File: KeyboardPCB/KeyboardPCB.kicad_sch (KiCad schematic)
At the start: 2 parts

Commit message: Made progress on keyboard schematic
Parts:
- added C? (x3): C, symbol Device:C
- added R? (x4): R, symbol Device:R
- added SW?: SW_Push, symbol Switch:SW_Push
- added Y?: Crystal_GND24_Small, symbol Device:Crystal_GND24_Small
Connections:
- net GND: now also U?.5 (UGND), C?.2, C?.2, C?.2, R?.1, SW?.1
- net at P?.A4 (VBUS), P?.A9 (VBUS), P?.B4 (VBUS)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: now also U?.2 (UVCC), U?.24 (AVCC), U?.44 (AVCC)
- net at U?.4 (D+): now also R?.1; no longer P?.A6 (D+)
- net at P?.A7 (D-): now also R?.2; no longer U?.3 (D-)
- net COL10: now reaches U?.1 (PE6)
- net COL1: now reaches U?.10 (PB2)
- net COL0: now reaches U?.11 (PB3)
- net ROW0: now reaches U?.12 (PB7)
- net at U?.13 (~{RESET}): now also R?.2
- net at U?.16 (XTAL2): now also C?.1, Y?.1
- net at U?.17 (XTAL1): now also C?.1, Y?.3
- net COL9: now reaches U?.18 (PD0)
- net COL8: now reaches U?.19 (PD1)
- net COL7: now reaches U?.20 (PD2)
- net COL6: now reaches U?.21 (PD3)
- net COL5: now reaches U?.22 (PD5)
- net COL19: now reaches U?.25 (PD4)
- net COL18: now reaches U?.26 (PD6)
- net COL17: now reaches U?.27 (PD7)
- net COL16: now reaches U?.28 (PB4)
- net COL15: now reaches U?.29 (PB5)
- net COL14: now reaches U?.30 (PB6)
- net COL13: now reaches U?.31 (PC6)
- net COL12: now reaches U?.32 (PC7)
- net at U?.33 (~{HWB}/PE2): now also R?.2
- net COL4: now reaches U?.36 (PF7)
- net ROW2: now reaches U?.37 (PF6)
- net ROW3: now reaches U?.38 (PF5)
- net ROW4: now reaches U?.39 (PF4)
- net ROW1: now reaches U?.40 (PF1)
- net COL11: now reaches U?.41 (PF0)
- net at U?.6 (UCAP): now also C?.1
- net COL3: now reaches U?.8 (PB0)
- net COL2: now reaches U?.9 (PB1)
- new net: R?.1, SW?.2
- new net: P?.A6 (D+), R?.2
- new net: R?.1, U?.3 (D-)
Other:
- moved on the sheet: P?, U?

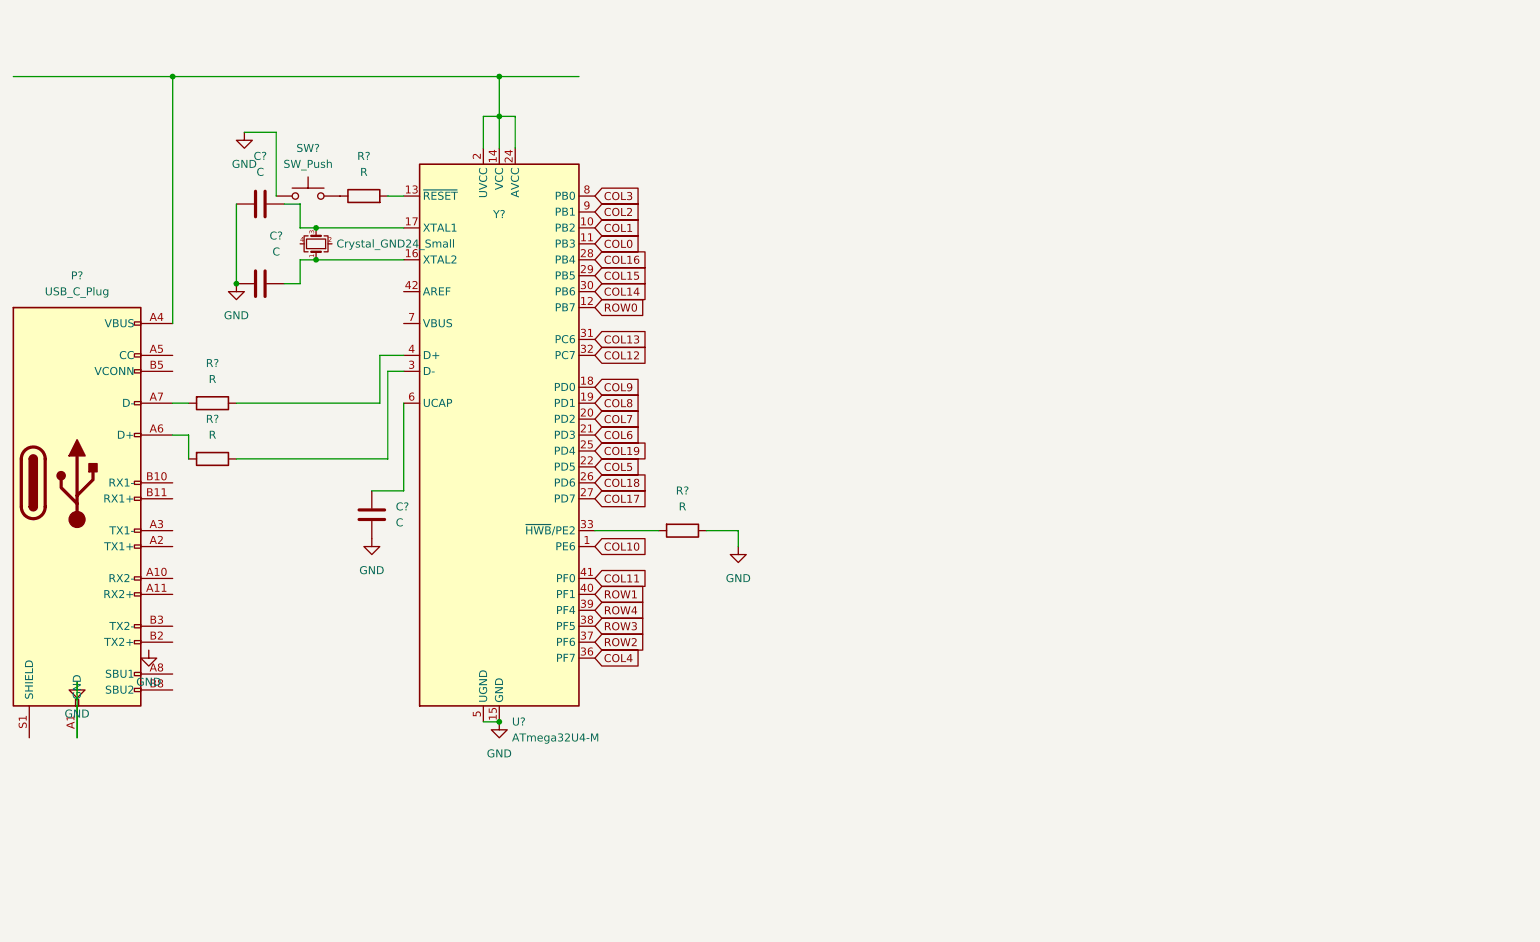
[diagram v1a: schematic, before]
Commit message: Added Sheets for main MCU/battery and key array
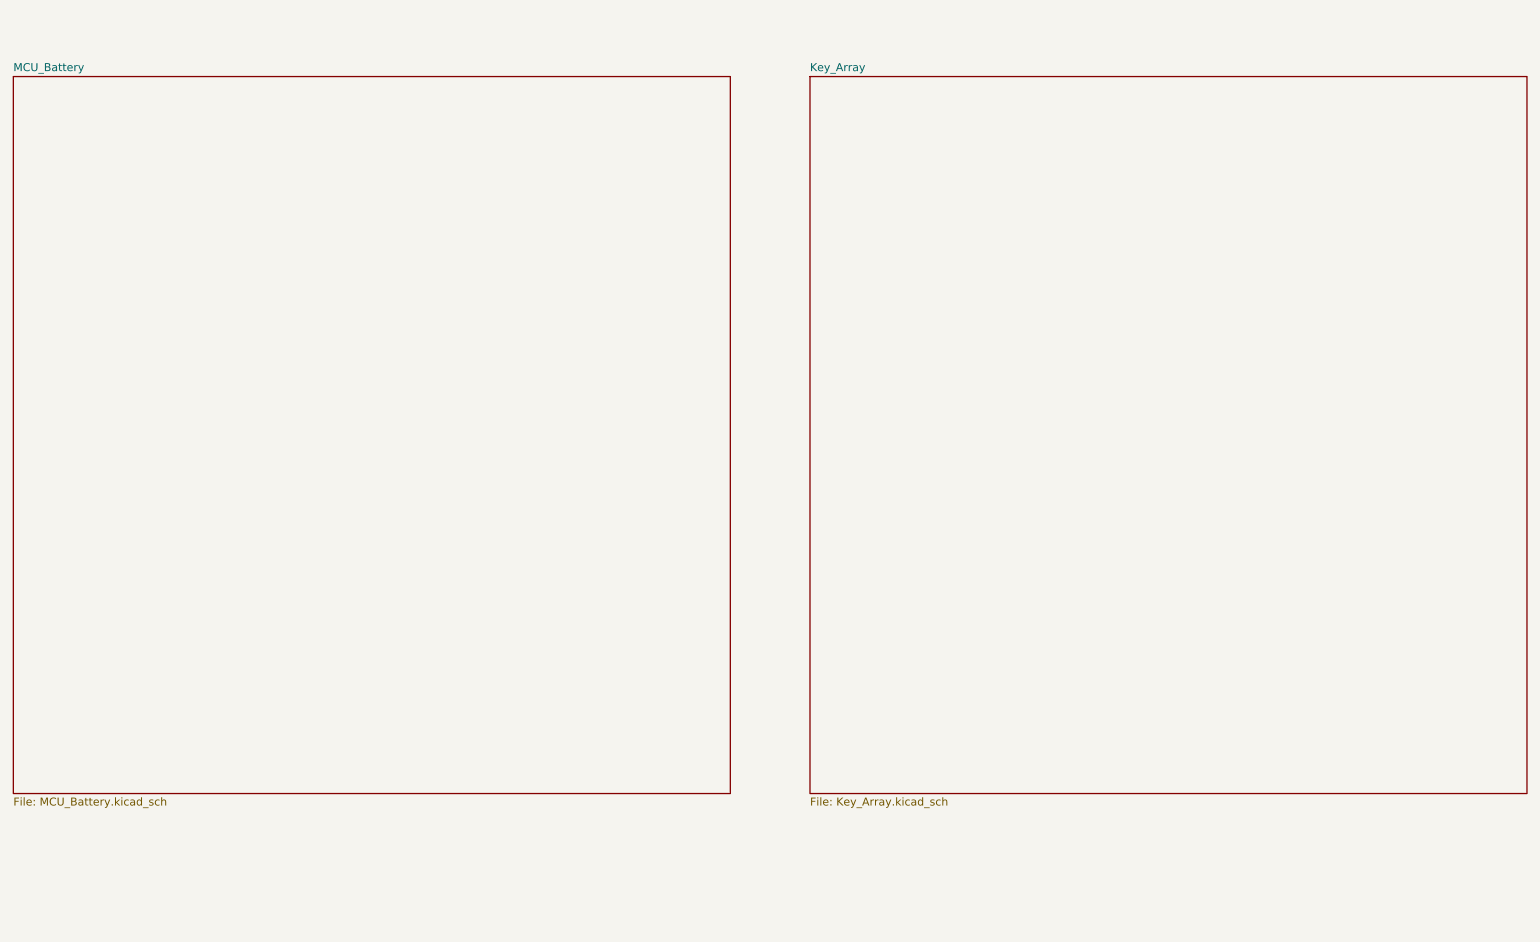
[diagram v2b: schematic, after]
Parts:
- removed C? (x3): C, symbol Device:C
- removed P?: USB_C_Plug, symbol Connector:USB_C_Plug
- removed R? (x4): R, symbol Device:R
- removed SW?: SW_Push, symbol Switch:SW_Push
- removed U?: ATmega32U4-M, Package_DFN_QFN:QFN-44-1EP_7x7mm_P0.5mm_EP5.2x5.2mm, symbol MCU_Microchip_ATmega:ATmega32U4-M
- removed Y?: Crystal_GND24_Small, symbol Device:Crystal_GND24_Small
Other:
- added sheet Key_Array (Key_Array.kicad_sch)
- added sheet MCU_Battery (MCU_Battery.kicad_sch)

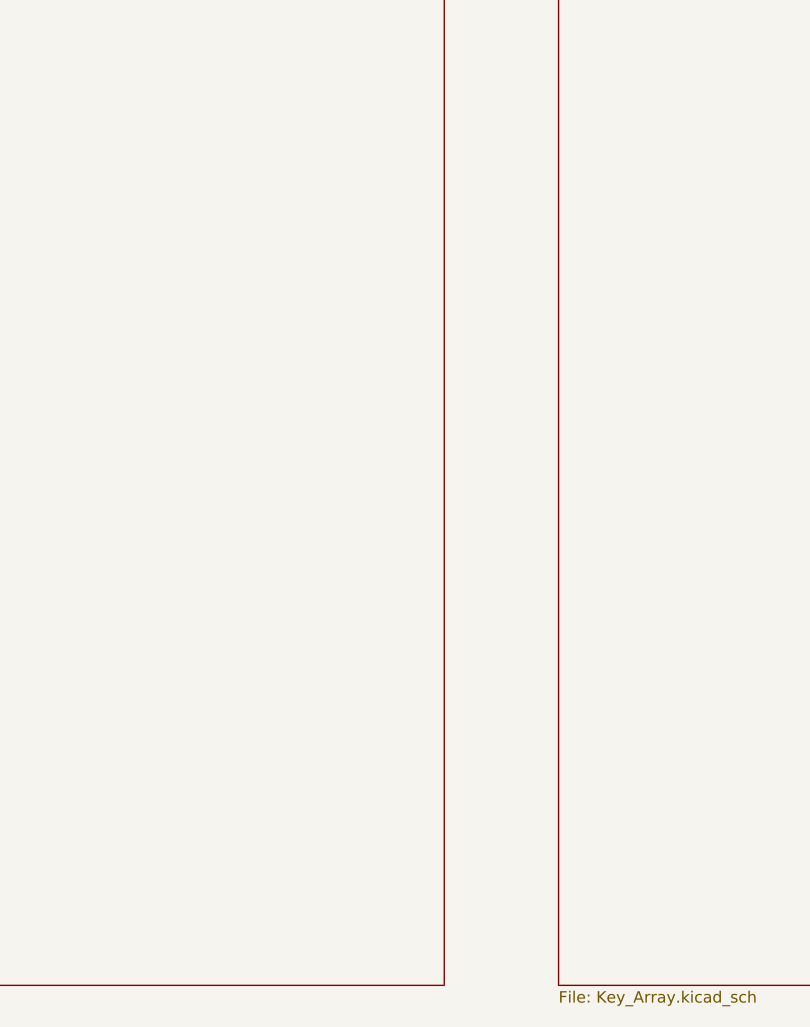
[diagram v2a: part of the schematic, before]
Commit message: set up for key array
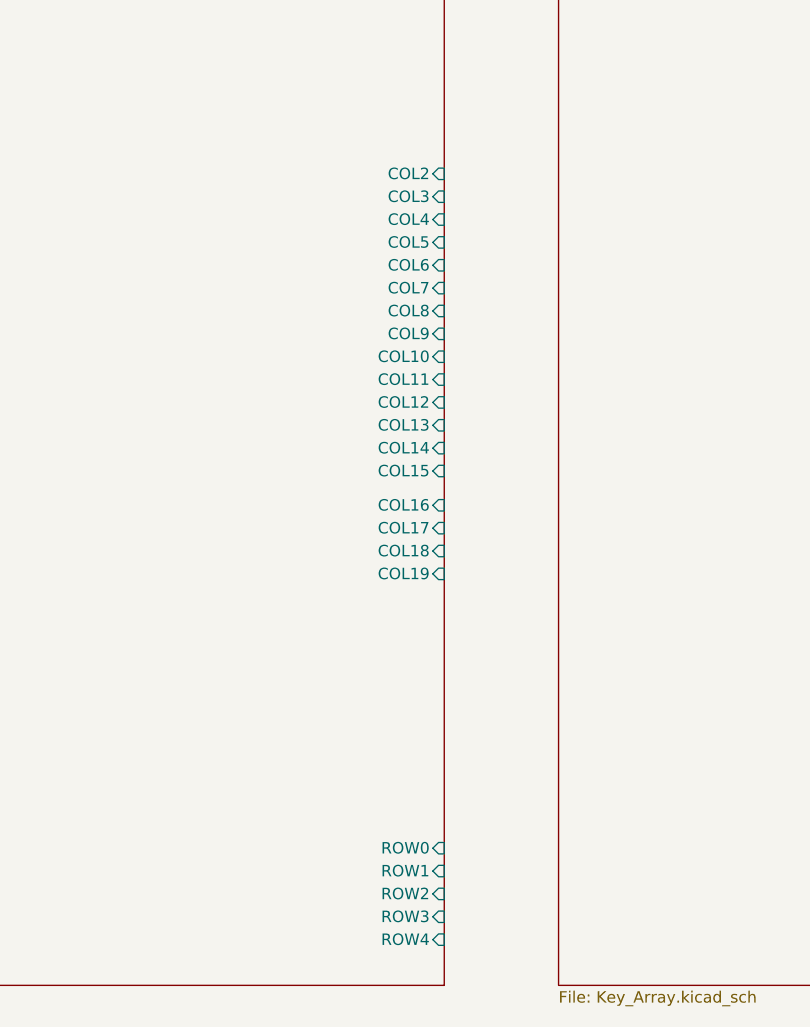
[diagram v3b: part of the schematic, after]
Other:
- sheet MCU_Battery ports: added COL10, COL11, COL12, COL13, COL14, COL15, COL16, COL17, COL18, COL19, COL2, COL3, COL4, COL5, COL6, COL7, COL8, COL9, ROW0, ROW1, ROW2, ROW3, ROW4; removed none
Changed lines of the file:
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@@
       (effects (font (size 1.27 1.27)) (justify left top))
+    )
+    (pin "COL3" input (at 139.7 52.07 0)
+      (effects (font (size 1.27 1.27)) (justify right))
+    )
+    (pin "ROW4" input (at 139.7 134.62 0)
+      (effects (font (size 1.27 1.27)) (justify right))
+    )
+    (pin "ROW1" input (at 139.7 127 0)
+      (effects (font (size 1.27 1.27)) (justify right))
+    )
+    (pin "COL11" input (at 139.7 72.39 0)
+      (effects (font (size 1.27 1.27)) (justify right))
+    )
+    (pin "COL18" input (at 139.7 91.44 0)
+      (effects (font (size 1.27 1.27)) (justify right))
+    )
+    (pin "COL10" input (at 139.7 69.85 0)
+      (effects (font (size 1.27 1.27)) (justify right))
+    )
+    (pin "COL17" input (at 139.7 88.9 0)
+      (effects (font (size 1.27 1.27)) (justify right))
+    )
+    (pin "COL5" input (at 139.7 57.15 0)
+      (effects (font (size 1.27 1.27)) (justify right))
+    )
+    (pin "COL7" input (at 139.7 62.23 0)
+      (effects (font (size 1.27 1.27)) (justify right))
+    )
+    (pin "COL6" input (at 139.7 59.69 0)
+      (effects (font (size 1.27 1.27)) (justify right))
+    )
+    (pin "COL19" input (at 139.7 93.98 0)
+      (effects (font (size 1.27 1.27)) (justify right))
+    )
+    (pin "COL8" input (at 139.7 64.77 0)
+      (effects (font (size 1.27 1.27)) (justify right))
+    )
+    (pin "ROW3" input (at 139.7 132.08 0)
+      (effects (font (size 1.27 1.27)) (justify right))
+    )
+    (pin "COL4" input (at 139.7 54.61 0)
+      (effects (font (size 1.27 1.27)) (justify right))
+    )
+    (pin "ROW2" input (at 139.7 129.54 0)
+      (effects (font (size 1.27 1.27)) (justify right))
+    )
+    (pin "ROW0" input (at 139.7 124.46 0)
+      (effects (font (size 1.27 1.27)) (justify right))
+    )
+    (pin "COL9" input (at 139.7 67.31 0)
+      (effects (font (size 1.27 1.27)) (justify right))
+    )
+    (pin "COL13" input (at 139.7 77.47 0)
+      (effects (font (size 1.27 1.27)) (justify right))
+    )
+    (pin "COL12" input (at 139.7 74.93 0)
+      (effects (font (size 1.27 1.27)) (justify right))
+    )
+    (pin "COL16" input (at 139.7 86.36 0)
+      (effects (font (size 1.27 1.27)) (justify right))
+    )
+    (pin "COL2" input (at 139.7 49.53 0)
+      (effects (font (size 1.27 1.27)) (justify right))
+    )
+    (pin "COL14" input (at 139.7 80.01 0)
+      (effects (font (size 1.27 1.27)) (justify right))
+    )
+    (pin "COL15" input (at 139.7 82.55 0)
+      (effects (font (size 1.27 1.27)) (justify right))
     )
   )
@@
       (reference "#PWR?") (unit 1) (value "GND") (footprint "")
     )
-    (path "/0e04ce72-6533-49cc-b4b5-6fa7ba1a6887/e65c3227-a683-4185-b179-fe03d95c6a0f"
-      (reference "#PWR?") (unit 1) (value "GND") (footprint "")
-    )
     (path "/0e04ce72-6533-49cc-b4b5-6fa7ba1a6887/f025268d-94e6-435c-9e99-144e0a25759e"
       (reference "#PWR?") (unit 1) (value "GND") (footprint "")
     )
+    (path "/0e04ce72-6533-49cc-b4b5-6fa7ba1a6887/f72b91bb-4963-49bc-9a06-44650fc96a66"
+      (reference "#PWR?") (unit 1) (value "GND") (footprint "")
+    )

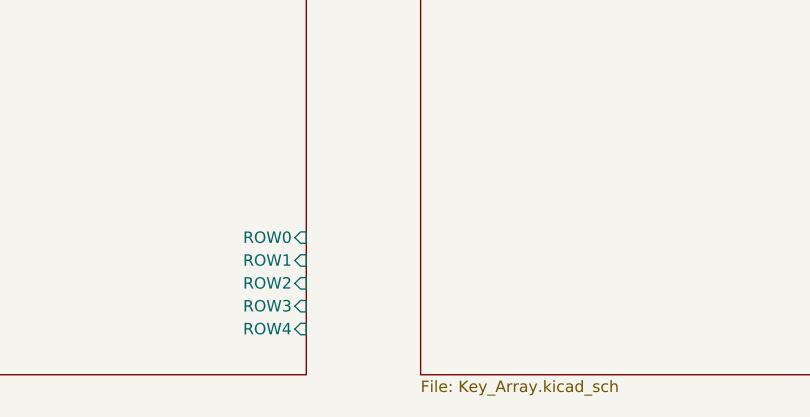
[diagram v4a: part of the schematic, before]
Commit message: keyboard added
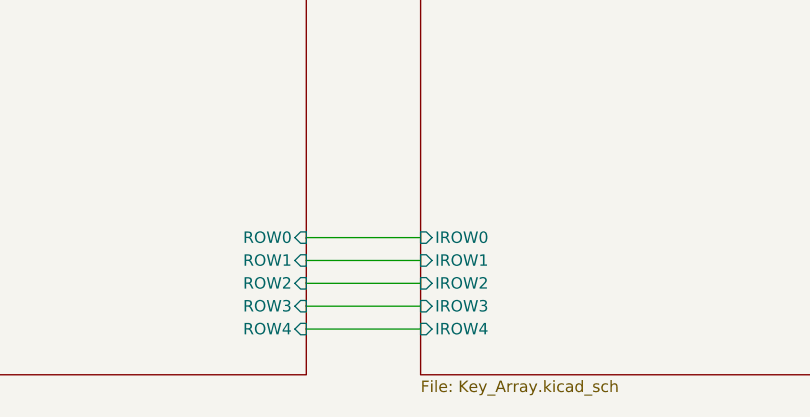
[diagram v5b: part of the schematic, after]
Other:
- sheet Key_Array ports: added IROW0, IROW1, IROW2, IROW3, IROW4; removed none
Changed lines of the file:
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@@
 (kicad_sch (version 20211123) (generator eeschema)
   (paper "A4")
+  (wire (pts (xy 139.7 129.54) (xy 152.4 129.54))
+    (stroke (width 0) (type default) (color 0 0 0 0))
+  )
+  (wire (pts (xy 139.7 127) (xy 152.4 127))
+    (stroke (width 0) (type default) (color 0 0 0 0))
+  )
+  (wire (pts (xy 139.7 134.62) (xy 152.4 134.62))
+    (stroke (width 0) (type default) (color 0 0 0 0))
+  )
+  (wire (pts (xy 139.7 132.08) (xy 152.4 132.08))
+    (stroke (width 0) (type default) (color 0 0 0 0))
+  )
+  (wire (pts (xy 139.7 124.46) (xy 152.4 124.46))
+    (stroke (width 0) (type default) (color 0 0 0 0))
+  )
   (sheet (at 25.4 25.4) (size 114.3 114.3) (fields_autoplaced)
     (stroke (width 0.1524) (type solid) (color 0 0 0 0))
@@
       (effects (font (size 1.27 1.27)) (justify left top))
     )
+    (pin "IROW3" input (at 152.4 132.08 180)
+      (effects (font (size 1.27 1.27)) (justify left))
+    )
+    (pin "IROW0" input (at 152.4 124.46 180)
+      (effects (font (size 1.27 1.27)) (justify left))
+    )
+    (pin "IROW1" input (at 152.4 127 180)
+      (effects (font (size 1.27 1.27)) (justify left))
+    )
+    (pin "IROW2" input (at 152.4 129.54 180)
+      (effects (font (size 1.27 1.27)) (justify left))
+    )
+    (pin "IROW4" input (at 152.4 134.62 180)
+      (effects (font (size 1.27 1.27)) (justify left))
+    )
   )
   (sheet_instances
@@
       (reference "C?") (unit 1) (value "C") (footprint "")
     )
+    (path "/ea7fdac0-4451-48b5-bbfd-e0f47d60ba04/085d0668-2bdd-442e-845c-04885261abc3"
+      (reference "D?") (unit 1) (value "1N4148WT") (footprint "Diode_SMD:D_SOD-523")
+    )
+    (path "/ea7fdac0-4451-48b5-bbfd-e0f47d60ba04/093654b7-9a4e-46ae-aec2-41e4a1ffa408"
+      (reference "D?") (unit 1) (value "1N4148WT") (footprint "Diode_SMD:D_SOD-523")
+    )
+    (path "/ea7fdac0-4451-48b5-bbfd-e0f47d60ba04/0d494db2-e686-41d9-88ce-34916737d604"
+      (reference "D?") (unit 1) (value "1N4148WT") (footprint "Diode_SMD:D_SOD-523")
+    )
+    (path "/ea7fdac0-4451-48b5-bbfd-e0f47d60ba04/16056eea-bff8-43e3-bb4c-e2e99df660e6"
+      (reference "D?") (unit 1) (value "1N4148WT") (footprint "Diode_SMD:D_SOD-523")
+    )
+    (path "/ea7fdac0-4451-48b5-bbfd-e0f47d60ba04/17a0798e-831d-48ea-bd0e-a352003521db"
+      (reference "D?") (unit 1) (value "1N4148WT") (footprint "Diode_SMD:D_SOD-523")
+    )
+    (path "/ea7fdac0-4451-48b5-bbfd-e0f47d60ba04/223d0d00-e7b6-435c-969f-835885c93655"
+      (reference "D?") (unit 1) (value "1N4148WT") (footprint "Diode_SMD:D_SOD-523")
+    )
+    (path "/ea7fdac0-4451-48b5-bbfd-e0f47d60ba04/41cf5a6e-7eaf-4a99-af9a-7c6d950a495f"
+      (reference "D?") (unit 1) (value "1N4148WT") (footprint "Diode_SMD:D_SOD-523")
+    )
+    (path "/ea7fdac0-4451-48b5-bbfd-e0f47d60ba04/431e94e4-692a-49ef-91fa-2f1556593f4e"
+      (reference "D?") (unit 1) (value "1N4148WT") (footprint "Diode_SMD:D_SOD-523")
+    )
+    (path "/ea7fdac0-4451-48b5-bbfd-e0f47d60ba04/501e12a6-9a36-4baf-80f5-810ca392bffd"
+      (reference "D?") (unit 1) (value "1N4148WT") (footprint "Diode_SMD:D_SOD-523")
+    )
+    (path "/ea7fdac0-4451-48b5-bbfd-e0f47d60ba04/5840ce00-bee4-40ba-846f-10ca1bb7d4de"
+      (reference "D?") (unit 1) (value "1N4148WT") (footprint "Diode_SMD:D_SOD-523")
+    )
+    (path "/ea7fdac0-4451-48b5-bbfd-e0f47d60ba04/5fa281b3-e577-4328-8d83-48a007938557"
+      (reference "D?") (unit 1) (value "1N4148WT") (footprint "Diode_SMD:D_SOD-523")
+    )
+    (path "/ea7fdac0-4451-48b5-bbfd-e0f47d60ba04/6ae57d11-2a31-46f4-8222-b0bd7d31568b"
+      (reference "D?") (unit 1) (value "1N4148WT") (footprint "Diode_SMD:D_SOD-523")
+    )
+    (path "/ea7fdac0-4451-48b5-bbfd-e0f47d60ba04/6da9421a-adbd-4537-9d56-f2db3ac939ed"
+      (reference "D?") (unit 1) (value "1N4148WT") (footprint "Diode_SMD:D_SOD-523")
+    )
+    (path "/ea7fdac0-4451-48b5-bbfd-e0f47d60ba04/71436118-c748-4905-af3d-df29f06c495c"
+      (reference "D?") (unit 1) (value "1N4148WT") (footprint "Diode_SMD:D_SOD-523")
+    )
+    (path "/ea7fdac0-4451-48b5-bbfd-e0f47d60ba04/92a1e4cf-9acd-481f-b88e-e8b9a265ecdf"
+      (reference "D?") (unit 1) (value "1N4148WT") (footprint "Diode_SMD:D_SOD-523")
+    )
+    (path "/ea7fdac0-4451-48b5-bbfd-e0f47d60ba04/97b7cdb2-0216-462b-905c-2660b2056218"
+      (reference "D?") (unit 1) (value "1N4148WT") (footprint "Diode_SMD:D_SOD-523")
+    )
+    (path "/ea7fdac0-4451-48b5-bbfd-e0f47d60ba04/a85d7478-307e-47f5-a60f-3f2421d1bcea"
+      (reference "D?") (unit 1) (value "1N4148WT") (footprint "Diode_SMD:D_SOD-523")
+    )
+    (path "/ea7fdac0-4451-48b5-bbfd-e0f47d60ba04/d176cf6e-56df-4a40-b93b-80e097893c73"
+      (reference "D?") (unit 1) (value "1N4148WT") (footprint "Diode_SMD:D_SOD-523")
+    )
+    (path "/ea7fdac0-4451-48b5-bbfd-e0f47d60ba04/e4268ceb-2678-4de9-a4ca-bddabb568869"
+      (reference "D?") (unit 1) (value "1N4148WT") (footprint "Diode_SMD:D_SOD-523")
+    )
+    (path "/ea7fdac0-4451-48b5-bbfd-e0f47d60ba04/e4fb8c8c-736b-44dc-b9ed-ef5ee728c773"
+      (reference "D?") (unit 1) (value "1N4148WT") (footprint "Diode_SMD:D_SOD-523")
+    )
+    (path "/ea7fdac0-4451-48b5-bbfd-e0f47d60ba04/e659915c-b451-4bb8-928a-9ba1a5963466"
+      (reference "D?") (unit 1) (value "1N4148WT") (footprint "Diode_SMD:D_SOD-523")
+    )
+    (path "/ea7fdac0-4451-48b5-bbfd-e0f47d60ba04/efa2639e-c29f-44ad-8c82-496ec26a1cee"
+      (reference "D?") (unit 1) (value "1N4148WT") (footprint "Diode_SMD:D_SOD-523")
+    )
+    (path "/ea7fdac0-4451-48b5-bbfd-e0f47d60ba04/f54334f0-73c8-4d3f-8db3-1519a520ddd0"
+      (reference "D?") (unit 1) (value "1N4148WT") (footprint "Diode_SMD:D_SOD-523")
+    )
     (path "/0e04ce72-6533-49cc-b4b5-6fa7ba1a6887/183f1189-1050-4e26-a66a-be7f0e46c29b"
